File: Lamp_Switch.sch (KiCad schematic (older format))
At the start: 11 parts

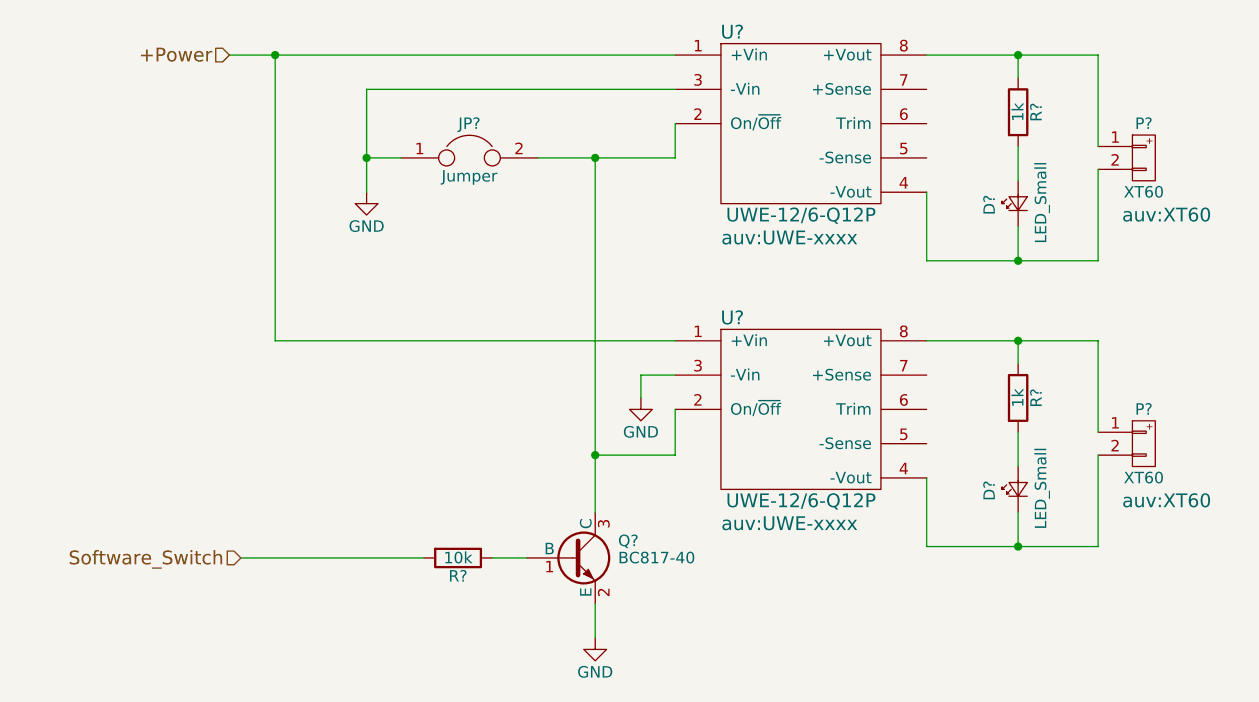
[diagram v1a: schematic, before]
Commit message: Correct all foot-print assignments
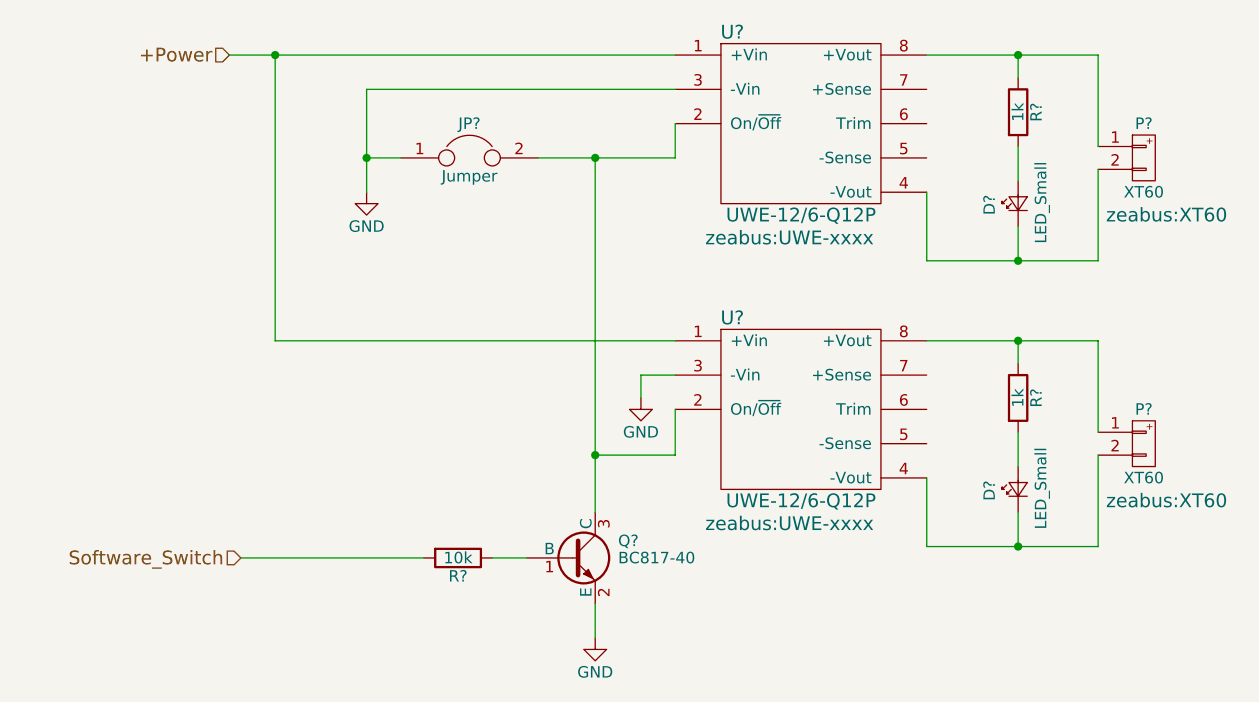
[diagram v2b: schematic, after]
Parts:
- P? (x2): footprint auv:XT60 -> zeabus:XT60
- U? (x2): footprint auv:UWE-xxxx -> zeabus:UWE-xxxx
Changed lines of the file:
@@
 $Descr A4 11693 8268
 encoding utf-8
-Sheet 3 12
+Sheet 3 13
 Title ""
 Date ""
@@
 F 0 "U?" H 5350 3300 60  0000 C CNN
 F 1 "UWE-12/6-Q12P" H 5650 2500 60  0000 C CNN
-F 2 "auv:UWE-xxxx" H 5600 2400 60  0000 C CNN
+F 2 "zeabus:UWE-xxxx" H 5600 2400 60  0000 C CNN
 F 3 "" H 5700 2600 60  0000 C CNN
 	1    5650 2900
@@
 F 0 "P?" H 7150 3200 50  0000 C CNN
 F 1 "XT60" H 7150 2900 50  0000 C CNN
-F 2 "auv:XT60" H 7250 2800 60  0000 C CNN
+F 2 "zeabus:XT60" H 7250 2800 60  0000 C CNN
 F 3 "" H 7150 3050 60  0000 C CNN
 	1    7150 3050
@@
 F 0 "U?" H 5350 4550 60  0000 C CNN
 F 1 "UWE-12/6-Q12P" H 5650 3750 60  0000 C CNN
-F 2 "auv:UWE-xxxx" H 5600 3650 60  0000 C CNN
+F 2 "zeabus:UWE-xxxx" H 5600 3650 60  0000 C CNN
 F 3 "" H 5700 3850 60  0000 C CNN
 	1    5650 4150
@@
 F 0 "P?" H 7150 4450 50  0000 C CNN
 F 1 "XT60" H 7150 4150 50  0000 C CNN
-F 2 "auv:XT60" H 7250 4050 60  0000 C CNN
+F 2 "zeabus:XT60" H 7250 4050 60  0000 C CNN
 F 3 "" H 7150 4300 60  0000 C CNN
 	1    7150 4300

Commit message: Annotate all components
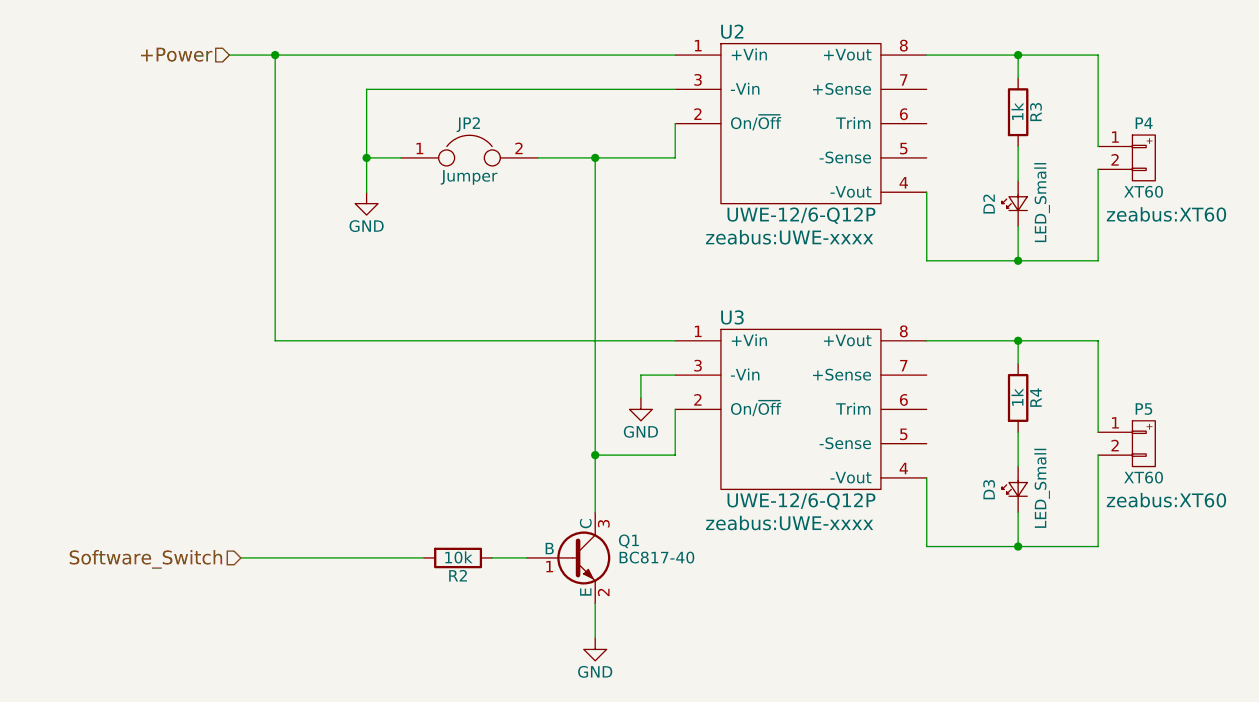
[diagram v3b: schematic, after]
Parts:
- gave numbers to parts that had none: 11
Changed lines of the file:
@@
 LIBS:zeabus
 LIBS:ftdi
-LIBS:Power_Distributor-cache
 EELAYER 25 0
 EELAYER END
@@
 $EndDescr
 $Comp
-L UWE-12/6-Q12P U?
+L UWE-12/6-Q12P U2
 U 1 1 58C998ED
 P 5650 2900
-F 0 "U?" H 5350 3300 60  0000 C CNN
+F 0 "U2" H 5350 3300 60  0000 C CNN
 F 1 "UWE-12/6-Q12P" H 5650 2500 60  0000 C CNN
 F 2 "zeabus:UWE-xxxx" H 5600 2400 60  0000 C CNN
@@
 $EndComp
 $Comp
-L LED_Small D?
+L LED_Small D2
 U 1 1 58C99970
 P 6600 3250
-F 0 "D?" H 6550 3375 50  0000 L CNN
+F 0 "D2" H 6550 3375 50  0000 L CNN
 F 1 "LED_Small" H 6425 3150 50  0000 L CNN
 F 2 "LEDs:LED_0603" V 6600 3250 50  0001 C CNN
@@
 $EndComp
 $Comp
-L R R?
+L R R3
 U 1 1 58C999A9
 P 6600 2850
-F 0 "R?" V 6680 2850 50  0000 C CNN
+F 0 "R3" V 6680 2850 50  0000 C CNN
 F 1 "1k" V 6600 2850 50  0000 C CNN
 F 2 "Resistors_SMD:R_0603" V 6530 2850 50  0001 C CNN
@@
 $EndComp
 $Comp
-L XT60 P?
+L XT60 P4
 U 1 1 58C999F4
 P 7150 3050
-F 0 "P?" H 7150 3200 50  0000 C CNN
+F 0 "P4" H 7150 3200 50  0000 C CNN
 F 1 "XT60" H 7150 2900 50  0000 C CNN
 F 2 "zeabus:XT60" H 7250 2800 60  0000 C CNN
@@
 $EndComp
 $Comp
-L GND #PWR?
+L GND #PWR014
 U 1 1 58C99AB8
 P 4750 5150
-F 0 "#PWR?" H 4750 4900 50  0001 C CNN
+F 0 "#PWR014" H 4750 4900 50  0001 C CNN
 F 1 "GND" H 4750 5000 50  0000 C CNN
 F 2 "" H 4750 5150 50  0001 C CNN
@@
 $EndComp
 $Comp
-L GND #PWR?
+L GND #PWR015
 U 1 1 58C99B05
 P 3750 3200
-F 0 "#PWR?" H 3750 2950 50  0001 C CNN
+F 0 "#PWR015" H 3750 2950 50  0001 C CNN
 F 1 "GND" H 3750 3050 50  0000 C CNN
 F 2 "" H 3750 3200 50  0001 C CNN
@@
 $EndComp
 $Comp
-L Jumper JP?
+L Jumper JP2
 U 1 1 58C99B23
 P 4200 3050
-F 0 "JP?" H 4200 3200 50  0000 C CNN
+F 0 "JP2" H 4200 3200 50  0000 C CNN
 F 1 "Jumper" H 4200 2970 50  0000 C CNN
 F 2 "Pin_Headers:Pin_Header_Straight_1x02_Pitch2.00mm" H 4200 3050 50  0001 C CNN
@@
 $EndComp
 $Comp
-L R R?
+L R R2
 U 1 1 58C9A382
 P 4150 4800
-F 0 "R?" V 4230 4800 50  0000 C CNN
+F 0 "R2" V 4230 4800 50  0000 C CNN
 F 1 "10k" V 4150 4800 50  0000 C CNN
 F 2 "Resistors_SMD:R_0603" V 4080 4800 50  0001 C CNN
@@
 Software_Switch
 $Comp
-L UWE-12/6-Q12P U?
+L UWE-12/6-Q12P U3
 U 1 1 58C9B4D5
 P 5650 4150
-F 0 "U?" H 5350 4550 60  0000 C CNN
+F 0 "U3" H 5350 4550 60  0000 C CNN
 F 1 "UWE-12/6-Q12P" H 5650 3750 60  0000 C CNN
 F 2 "zeabus:UWE-xxxx" H 5600 3650 60  0000 C CNN
@@
 	3350 3850 5100 3850
 $Comp
-L GND #PWR?
+L GND #PWR016
 U 1 1 58C9C409
 P 4950 4100
-F 0 "#PWR?" H 4950 3850 50  0001 C CNN
+F 0 "#PWR016" H 4950 3850 50  0001 C CNN
 F 1 "GND" H 4950 3950 50  0000 C CNN
 F 2 "" H 4950 4100 50  0001 C CNN
@@
 	4950 4000 4950 4100
 $Comp
-L XT60 P?
+L XT60 P5
 U 1 1 58C9E70C
 P 7150 4300
-F 0 "P?" H 7150 4450 50  0000 C CNN
+F 0 "P5" H 7150 4450 50  0000 C CNN
 F 1 "XT60" H 7150 4150 50  0000 C CNN
 F 2 "zeabus:XT60" H 7250 4050 60  0000 C CNN
@@
 $EndComp
 $Comp
-L R R?
+L R R4
 U 1 1 58C9E767
 P 6600 4100
-F 0 "R?" V 6680 4100 50  0000 C CNN
+F 0 "R4" V 6680 4100 50  0000 C CNN
 F 1 "1k" V 6600 4100 50  0000 C CNN
 F 2 "Resistors_SMD:R_0603" V 6530 4100 50  0001 C CNN
@@
 $EndComp
 $Comp
-L LED_Small D?
+L LED_Small D3
 U 1 1 58C9E7BF
 P 6600 4500
-F 0 "D?" H 6550 4625 50  0000 L CNN
+F 0 "D3" H 6550 4625 50  0000 L CNN
 F 1 "LED_Small" H 6425 4400 50  0000 L CNN
 F 2 "LEDs:LED_0603" V 6600 4500 50  0001 C CNN
@@
 Connection ~ 6600 4750
 $Comp
-L BC817-40 Q?
+L BC817-40 Q1
 U 1 1 58E56DE9
 P 4650 4800
-F 0 "Q?" H 4850 4875 50  0000 L CNN
+F 0 "Q1" H 4850 4875 50  0000 L CNN
 F 1 "BC817-40" H 4850 4800 50  0000 L CNN
 F 2 "TO_SOT_Packages_SMD:SOT-23" H 4850 4725 50  0001 L CIN
